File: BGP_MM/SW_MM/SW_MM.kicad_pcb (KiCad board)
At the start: 2 copper layers, 17 x 13 mm, 2 parts, among them P1 CONN_01X04, SW1 Switch_SPDT_x2

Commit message: MM Tweaks
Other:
- board text added: "MM Sabre Coil Switch CBD Design"
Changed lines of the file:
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@@
     (links 5)
     (no_connects 0)
-    (area 136.526099 95.778599 150.476101 113.225001)
+    (area 136.778599 82.523899 154.225001 96.473901)
     (thickness 1.6)
-    (drawings 4)
+    (drawings 5)
     (tracks 13)
     (zones 0)
@@
     )
   )
+  (gr_text "MM Sabre\nCoil Switch\nCBD Design" (at 138.8 87.5 270) (layer B.SilkS)
+    (effects (font (size 0.6 0.6) (thickness 0.15)))
+  )
   (gr_line (start 154 96) (end 137 96) (layer Edge.Cuts) (width 0.15))

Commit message: MM Switches and BOM
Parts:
- moved P1 1.10 mm to (150.6, 92.5)
- moved SW1 0.80 mm to (145.2, 84.8)
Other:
- board size 17 x 13 mm -> 16 x 13 mm
- board text added: "MM Sabre Coil Switch"
- board text removed: "MM Sabre Coil Switch CBD Design"
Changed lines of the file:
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@@
   (general
     (links 5)
-    (no_connects 0)
-    (area 136.778599 82.523899 154.225001 96.473901)
+    (no_connects 5)
+    (area 136.924999 82.924999 154.075001 96.075001)
     (thickness 1.6)
     (drawings 5)
-    (tracks 13)
+    (tracks 14)
     (zones 0)
     (modules 2)
@@
     (add_net "Net-(SW1-Pad6)")
   )
-  (module LIBS:NKK_DPDT (layer F.Cu)
-    (at 146.0036 84.7989 90)
-    (descr "2-way 2.54mm pitch terminal block, Phoenix MPT series")
-    (fp_text reference SW1 (at -4.6011 -2.1036 270) (layer F.SilkS)
-      (effects (font (size 1 1) (thickness 0.15)))
-    )
-    (fp_text value Switch_SPDT_x2 (at -4.45 5.2 90) (layer F.Fab) hide
-      (effects (font (size 1 1) (thickness 0.15)))
-    )
-    (fp_text user %R (at -4.6011 -2.1036 90) (layer F.Fab) hide
-      (effects (font (size 1 1) (thickness 0.15)))
-    )
-    (fp_line (start 1.95 4.1) (end -11.35 4.1) (layer F.CrtYd) (width 0.05))
-    (fp_line (start 1.95 -8.9) (end 1.95 4.1) (layer F.CrtYd) (width 0.05))
-    (fp_line (start -11.346872 -8.899165) (end 1.95 -8.9) (layer F.CrtYd) (width 0.05))
-    (fp_line (start -11.35 4.1) (end -11.35 -8.9) (layer F.CrtYd) (width 0.05))
-    (fp_line (start 1.8 -8.75) (end -11.2 -8.75) (layer F.SilkS) (width 0.15))
-    (fp_line (start -11.2 -8.75) (end -11.2 3.95) (layer F.SilkS) (width 0.15))
-    (fp_line (start -11.2 3.95) (end 1.8 3.95) (layer F.SilkS) (width 0.15))
-    (fp_line (start 1.8 3.95) (end 1.8 -8.75) (layer F.SilkS) (width 0.15))
-    (pad 5 thru_hole oval (at -4.7 -4.8 270) (size 1.8 1.8) (drill 1) (layers *.Cu *.Mask)
-      (net 1 /NC))
-    (pad 4 thru_hole circle (at 0 -4.8 270) (size 1.8 1.8) (drill 1) (layers *.Cu *.Mask)
-      (net 3 /BC))
-    (pad 6 thru_hole oval (at -9.4 -4.8 270) (size 1.8 1.8) (drill 1) (layers *.Cu *.Mask)
-      (net 5 "Net-(SW1-Pad6)"))
-    (pad 1 thru_hole circle (at 0 0.03 270) (size 1.8 1.8) (drill 1) (layers *.Cu *.Mask)
-      (net 4 /BH))
-    (pad 2 thru_hole oval (at -4.7 0.03 270) (size 1.8 1.8) (drill 1) (layers *.Cu *.Mask)
-      (net 2 /NH))
-    (pad 3 thru_hole oval (at -9.4 0.03 270) (size 1.8 1.8) (drill 1) (layers *.Cu *.Mask)
-      (net 3 /BC))
-    (model ${KISYS3DMOD}/TerminalBlock_Phoenix.3dshapes/TerminalBlock_Phoenix_MPT-2.54mm_2pol.wrl
-      (at (xyz 0.05 0 0))
-      (scale (xyz 1 1 1))
-      (rotate (xyz 0 0 0))
-    )
-  )
   (module Connectors_JST:JST_PH_B4B-PH-K_04x2.00mm_Straight (layer B.Cu)
-    (at 151.7 92.4 90)
+    (at 150.6 92.5 90)
     (descr "JST PH series connector, B4B-PH-K, top entry type, through hole, Datasheet: http://www.jst-mfg.com/product/pdf/eng/ePH.pdf")
     (tags "connector jst ph")
@@
     )
   )
-  (gr_text "MM Sabre\nCoil Switch\nCBD Design" (at 138.8 87.5 270) (layer B.SilkS)
+  (module LIBS:NKK_DPDT (layer F.Cu)
+    (at 145.2 84.8 90)
+    (descr "2-way 2.54mm pitch terminal block, Phoenix MPT series")
+    (fp_text reference SW1 (at -5.1 -2.2 270) (layer F.SilkS)
+      (effects (font (size 1 1) (thickness 0.15)))
+    )
+    (fp_text value Switch_SPDT_x2 (at -4.45 4.55 90) (layer F.Fab) hide
+      (effects (font (size 1 1) (thickness 0.15)))
+    )
+    (fp_text user %R (at -5.1 -2.2 270) (layer F.Fab)
+      (effects (font (size 1 1) (thickness 0.15)))
+    )
+    (fp_line (start 1.8 3.45) (end -11.2 3.45) (layer F.CrtYd) (width 0.05))
+    (fp_line (start 1.8 -8.25) (end 1.8 3.45) (layer F.CrtYd) (width 0.05))
+    (fp_line (start -11.2 -8.25) (end 1.8 -8.25) (layer F.CrtYd) (width 0.05))
+    (fp_line (start -11.2 3.45) (end -11.2 -8.25) (layer F.CrtYd) (width 0.05))
+    (fp_line (start 1.65 -8.1) (end -11.05 -8.1) (layer F.SilkS) (width 0.15))
+    (fp_line (start -11.05 -8.1) (end -11.05 3.3) (layer F.SilkS) (width 0.15))
+    (fp_line (start -11.05 3.3) (end 1.65 3.3) (layer F.SilkS) (width 0.15))
+    (fp_line (start 1.65 3.3) (end 1.65 -8.1) (layer F.SilkS) (width 0.15))
+    (pad 5 thru_hole oval (at -4.7 -4.8 270) (size 1.8 1.8) (drill 1) (layers *.Cu *.Mask)
+      (net 1 /NC))
+    (pad 4 thru_hole circle (at 0 -4.8 270) (size 1.8 1.8) (drill 1) (layers *.Cu *.Mask)
+      (net 3 /BC))
+    (pad 6 thru_hole oval (at -9.4 -4.8 270) (size 1.8 1.8) (drill 1) (layers *.Cu *.Mask)
+      (net 5 "Net-(SW1-Pad6)"))
+    (pad 1 thru_hole circle (at 0 0.03 270) (size 1.8 1.8) (drill 1) (layers *.Cu *.Mask)
+      (net 4 /BH))
+    (pad 2 thru_hole oval (at -4.7 0.03 270) (size 1.8 1.8) (drill 1) (layers *.Cu *.Mask)
+      (net 2 /NH))
+    (pad 3 thru_hole oval (at -9.4 0.03 270) (size 1.8 1.8) (drill 1) (layers *.Cu *.Mask)
+      (net 3 /BC))
+    (model ${KISYS3DMOD}/TerminalBlock_Phoenix.3dshapes/TerminalBlock_Phoenix_MPT-2.54mm_2pol.wrl
+      (at (xyz 0.05 0 0))
+      (scale (xyz 1 1 1))
+      (rotate (xyz 0 0 0))
+    )
+  )
+  (gr_text "MM Sabre\nCoil Switch" (at 138.3 87.5 270) (layer B.SilkS)
     (effects (font (size 0.6 0.6) (thickness 0.15)))
   )
-  (gr_line (start 154 96) (end 137 96) (layer Edge.Cuts) (width 0.15))
-  (gr_line (start 154 83) (end 154 96) (layer Edge.Cuts) (width 0.15))
-  (gr_line (start 137 83) (end 154 83) (layer Edge.Cuts) (width 0.15))
+  (gr_line (start 153 96) (end 137 96) (layer Edge.Cuts) (width 0.15))
+  (gr_line (start 153 83) (end 153 96) (layer Edge.Cuts) (width 0.15))
+  (gr_line (start 137 83) (end 153 83) (layer Edge.Cuts) (width 0.15))
   (gr_line (start 137 96) (end 137 83) (layer Edge.Cuts) (width 0.15))
-  (segment (start 151.7 92.4) (end 144.1047 92.4) (width 0.5) (layer F.Cu) (net 1))
-  (segment (start 144.1047 92.4) (end 141.2036 89.4989) (width 0.5) (layer F.Cu) (net 1))
-  (segment (start 151.7 90.4) (end 146.9347 90.4) (width 0.5) (layer F.Cu) (net 2))
-  (segment (start 146.9347 90.4) (end 146.0336 89.4989) (width 0.5) (layer F.Cu) (net 2))
-  (segment (start 151.7 88.4) (end 150.1 88.4) (width 0.5) (layer B.Cu) (net 3))
-  (segment (start 150.1 88.4) (end 149.0953 87.3953) (width 0.5) (layer B.Cu) (net 3))
-  (segment (start 149.0953 87.3953) (end 143.8 87.3953) (width 0.5) (layer B.Cu) (net 3))
-  (segment (start 146.0336 94.1989) (end 143.8 91.9653) (width 0.5) (layer B.Cu) (net 3))
-  (segment (start 143.8 91.9653) (end 143.8 87.3953) (width 0.5) (layer B.Cu) (net 3))
-  (segment (start 143.8 87.3953) (end 142.103599 85.698899) (width 0.5) (layer B.Cu) (net 3))
-  (segment (start 142.103599 85.698899) (end 141.2036 84.7989) (width 0.5) (layer B.Cu) (net 3))
-  (segment (start 151.7 86.4) (end 147.6347 86.4) (width 0.5) (layer F.Cu) (net 4))
-  (segment (start 147.6347 86.4) (end 146.0336 84.7989) (width 0.5) (layer F.Cu) (net 4))
+  (segment (start 150.6 92.5) (end 143.4 92.5) (width 0.5) (layer B.Cu) (net 1))
+  (segment (start 143.4 92.5) (end 140.4 89.5) (width 0.5) (layer B.Cu) (net 1))
+  (segment (start 150.6 90.5) (end 146.23 90.5) (width 0.5) (layer B.Cu) (net 2))
+  (segment (start 146.23 90.5) (end 145.23 89.5) (width 0.5) (layer B.Cu) (net 2))
+  (segment (start 150.6 88.5) (end 149.25 88.5) (width 0.5) (layer F.Cu) (net 3))
+  (segment (start 149.25 88.5) (end 147.9 89.85) (width 0.5) (layer F.Cu) (net 3))
+  (segment (start 147.9 89.85) (end 147.9 91.5) (width 0.5) (layer F.Cu) (net 3))
+  (segment (start 147.9 91.5) (end 145.23 94.17) (width 0.5) (layer F.Cu) (net 3))
+  (segment (start 145.23 94.17) (end 145.23 94.2) (width 0.5) (layer F.Cu) (net 3))
+  (segment (start 143 87.4) (end 143 91.97) (width 0.5) (layer F.Cu) (net 3))
+  (segment (start 143 91.97) (end 145.23 94.2) (width 0.5) (layer F.Cu) (net 3))
+  (segment (start 140.4 84.8) (end 143 87.4) (width 0.5) (layer F.Cu) (net 3))
+  (segment (start 150.6 86.5) (end 146.93 86.5) (width 0.5) (layer F.Cu) (net 4))
+  (segment (start 146.93 86.5) (end 145.23 84.8) (width 0.5) (layer F.Cu) (net 4))
   (zone (net 0) (net_name "") (layer F.Cu) (hatch edge 0.508)
     (connect_pads (clearance 0.3))
@@
     (polygon
       (pts
-        (xy 137 96) (xy 137 83) (xy 154 83) (xy 154 96)
+        (xy 137 96) (xy 137 83) (xy 153 83) (xy 153 96)
       )
     )
@@
     (polygon
       (pts
-        (xy 137 96) (xy 137 83) (xy 154 83) (xy 154 96)
+        (xy 137 96) (xy 137 83) (xy 153 83) (xy 153 96)
       )
     )

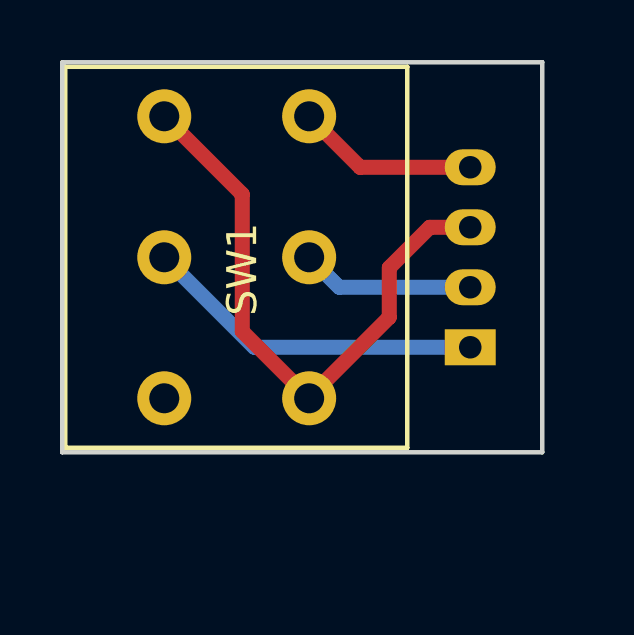
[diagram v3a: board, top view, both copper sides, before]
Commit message: MM Switch Config Changed
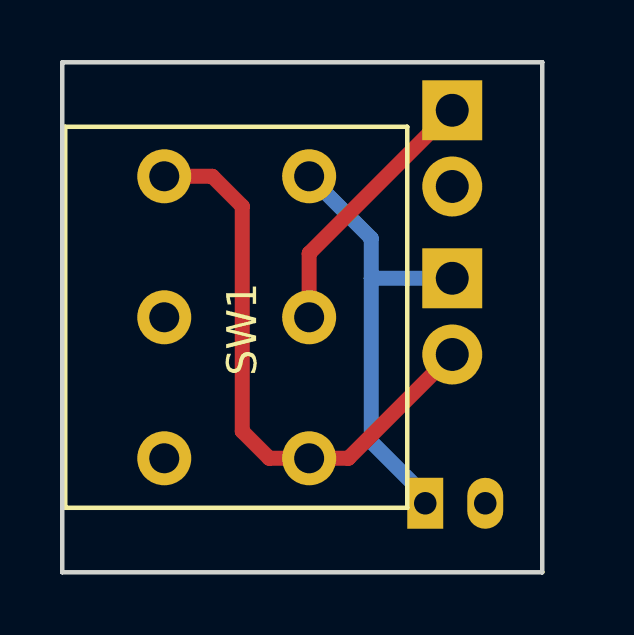
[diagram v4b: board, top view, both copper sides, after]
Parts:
- removed P1: CONN_01X04, Connectors_JST:JST_PH_B4B-PH-K_04x2.00mm_Straight
- added J1: Screw_Terminal_01x02, LIBS:TerminalBlock_Phoenix_MPT-2.54mm_2pol, B.Cu at (150.0, 84.6)
- added J2: Screw_Terminal_01x02, LIBS:TerminalBlock_Phoenix_MPT-2.54mm_2pol, B.Cu at (150.0, 90.2)
- added J3: Conn_01x02_Male, Connectors_JST:JST_PH_B2B-PH-K_02x2.00mm_Straight, B.Cu at (149.1, 97.7)
- SW1: value Switch_SPDT_x2 -> SW_DPDT_x2
- moved SW1 2.00 mm to (145.2, 86.8)
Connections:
- SW1 pad 5: /NC -> Earth
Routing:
- net /NC: track 11.4 -> 0.00 mm
- net /BH: track 6.07 -> 15.2 mm
- net /NH: track 5.78 -> 8.88 mm
- net /BC: track 20.1 -> 19.3 mm
- added copper zone on B.Cu, net Earth
- added copper zone on F.Cu, net Earth
- removed copper zone on B.Cu, net (none)
- removed copper zone on F.Cu, net (none)
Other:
- board size 16 x 13 mm -> 16 x 17 mm
